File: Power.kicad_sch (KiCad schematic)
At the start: 26 parts, among them SW1 SHPHLD, U1 NPM1304-QEAA-R

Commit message: Changed a few preferences
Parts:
- C1, C10, C11, C2, C5, C6, C7, C8, C9: footprint Capacitor_SMD:C_1206_3216Metric_Pad1.33x1.80mm_HandSolder -> Capacitor_SMD:C_0603_1608Metric
- D1, D2, D3: footprint LED_SMD:LED_1206_3216Metric_Pad1.42x1.75mm_HandSolder -> LED_SMD:LED_0603_1608Metric
- R1, R10, R2, R3, R7, R8, R9: footprint Resistor_SMD:R_1206_3216Metric_Pad1.30x1.75mm_HandSolder -> Resistor_SMD:R_0603_1608Metric
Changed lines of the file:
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@@
 			)
 		)
-		(property "Footprint" "Capacitor_SMD:C_1206_3216Metric_Pad1.33x1.80mm_HandSolder"
+		(property "Footprint" "Capacitor_SMD:C_0603_1608Metric"
 			(at 214.3252 100.33 0)
 			(hide yes)
@@
 			)
 		)
-		(property "Footprint" "Resistor_SMD:R_1206_3216Metric_Pad1.30x1.75mm_HandSolder"
+		(property "Footprint" "Resistor_SMD:R_0603_1608Metric"
 			(at 203.2 81.28 0)
 			(hide yes)
@@
 			)
 		)
-		(property "Footprint" "Capacitor_SMD:C_1206_3216Metric_Pad1.33x1.80mm_HandSolder"
+		(property "Footprint" "Capacitor_SMD:C_0603_1608Metric"
 			(at 195.2752 58.42 0)
 			(hide yes)
@@
 			)
 		)
-		(property "Footprint" "Capacitor_SMD:C_1206_3216Metric_Pad1.33x1.80mm_HandSolder"
+		(property "Footprint" "Capacitor_SMD:C_0603_1608Metric"
 			(at 223.52 143.2052 0)
 			(hide yes)
@@
 			)
 		)
-		(property "Footprint" "LED_SMD:LED_1206_3216Metric_Pad1.42x1.75mm_HandSolder"
+		(property "Footprint" "LED_SMD:LED_0603_1608Metric"
 			(at 193.04 73.66 90)
 			(hide yes)
@@
 			)
 		)
-		(property "Footprint" "Resistor_SMD:R_1206_3216Metric_Pad1.30x1.75mm_HandSolder"
+		(property "Footprint" "Resistor_SMD:R_0603_1608Metric"
 			(at 106.172 107.95 90)
 			(hide yes)
@@
 			)
 		)
-		(property "Footprint" "Capacitor_SMD:C_1206_3216Metric_Pad1.33x1.80mm_HandSolder"
+		(property "Footprint" "Capacitor_SMD:C_0603_1608Metric"
 			(at 98.7552 81.28 0)
 			(hide yes)
@@
 			)
 		)
-		(property "Footprint" "Capacitor_SMD:C_1206_3216Metric_Pad1.33x1.80mm_HandSolder"
+		(property "Footprint" "Capacitor_SMD:C_0603_1608Metric"
 			(at 223.52 132.3848 0)
 			(hide yes)
@@
 			)
 		)
-		(property "Footprint" "Capacitor_SMD:C_1206_3216Metric_Pad1.33x1.80mm_HandSolder"
+		(property "Footprint" "Capacitor_SMD:C_0603_1608Metric"
 			(at 237.1852 100.33 0)
 			(hide yes)
@@
 			)
 		)
-		(property "Footprint" "Capacitor_SMD:C_1206_3216Metric_Pad1.33x1.80mm_HandSolder"
+		(property "Footprint" "Capacitor_SMD:C_0603_1608Metric"
 			(at 94.9452 63.5 0)
 			(hide yes)
@@
 			)
 		)
-		(property "Footprint" "Resistor_SMD:R_1206_3216Metric_Pad1.30x1.75mm_HandSolder"
+		(property "Footprint" "Resistor_SMD:R_0603_1608Metric"
 			(at 203.2 88.9 0)
 			(hide yes)
@@
 			)
 		)
-		(property "Footprint" "Resistor_SMD:R_1206_3216Metric_Pad1.30x1.75mm_HandSolder"
+		(property "Footprint" "Resistor_SMD:R_0603_1608Metric"
 			(at 177.292 110.49 90)
 			(hide yes)
@@
 			)
 		)
-		(property "Footprint" "LED_SMD:LED_1206_3216Metric_Pad1.42x1.75mm_HandSolder"
+		(property "Footprint" "LED_SMD:LED_0603_1608Metric"
 			(at 193.04 88.9 90)
 			(hide yes)
@@
 			)
 		)
-		(property "Footprint" "Capacitor_SMD:C_1206_3216Metric_Pad1.33x1.80mm_HandSolder"
+		(property "Footprint" "Capacitor_SMD:C_0603_1608Metric"
 			(at 225.7552 100.33 0)
 			(hide yes)
@@
 			)
 		)
-		(property "Footprint" "Resistor_SMD:R_1206_3216Metric_Pad1.30x1.75mm_HandSolder"
+		(property "Footprint" "Resistor_SMD:R_0603_1608Metric"
 			(at 83.312 102.87 90)
 			(hide yes)
@@
 			)
 		)
-		(property "Footprint" "LED_SMD:LED_1206_3216Metric_Pad1.42x1.75mm_HandSolder"
+		(property "Footprint" "LED_SMD:LED_0603_1608Metric"
 			(at 193.04 81.28 90)
 			(hide yes)
@@
 			)
 		)
-		(property "Footprint" "Resistor_SMD:R_1206_3216Metric_Pad1.30x1.75mm_HandSolder"
+		(property "Footprint" "Resistor_SMD:R_0603_1608Metric"
 			(at 75.692 102.87 90)
 			(hide yes)
@@
 			)
 		)
-		(property "Footprint" "Resistor_SMD:R_1206_3216Metric_Pad1.30x1.75mm_HandSolder"
+		(property "Footprint" "Resistor_SMD:R_0603_1608Metric"
 			(at 203.2 73.66 0)
 			(hide yes)
@@
 			)
 		)
-		(property "Footprint" "Capacitor_SMD:C_1206_3216Metric_Pad1.33x1.80mm_HandSolder"
+		(property "Footprint" "Capacitor_SMD:C_0603_1608Metric"
 			(at 162.56 133.0452 0)
 			(hide yes)

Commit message: Finished preliminary project schematics and architecture
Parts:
- NT1, NT2: footprint NetTie:NetTie-2_SMD_Pad0.5mm -> NetTie:NetTie-2_SMD_Pad2.0mm
- renumbered C1 to C3, C2 to C4, L1 to L2, L2 to L3, R7 to R4, R8 to R5, R9 to R6, R10 to R7, U1 to U3
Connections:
- net NTC is gone; now on net GND: U3.18 (NTC)

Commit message: Edited ci.yaml
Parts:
- removed BT1: 1S Lipo, Connector_JST:JST_XH_B2B-XH-A_1x02_P2.50mm_Vertical, symbol Device:Battery_Cell
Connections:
- net CC1: now also U3.23 (CC1); no longer U3.24 (CC2)
- net CC2: now also U3.24 (CC2); no longer U3.23 (CC1)

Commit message: Cleaned up
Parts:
- renumbered C11 to C10, C5 to C11, C8 to C12, C9 to C13, C6 to C5, C3 to C6, C4 to C7, C7 to C8, C10 to C9, L3 to L2, L2 to L3, R4 to R10, R5 to R4, R6 to R5, R7 to R6, R1 to R7, R2 to R8, R3 to R9, SW1 to SW3, U3 to U2

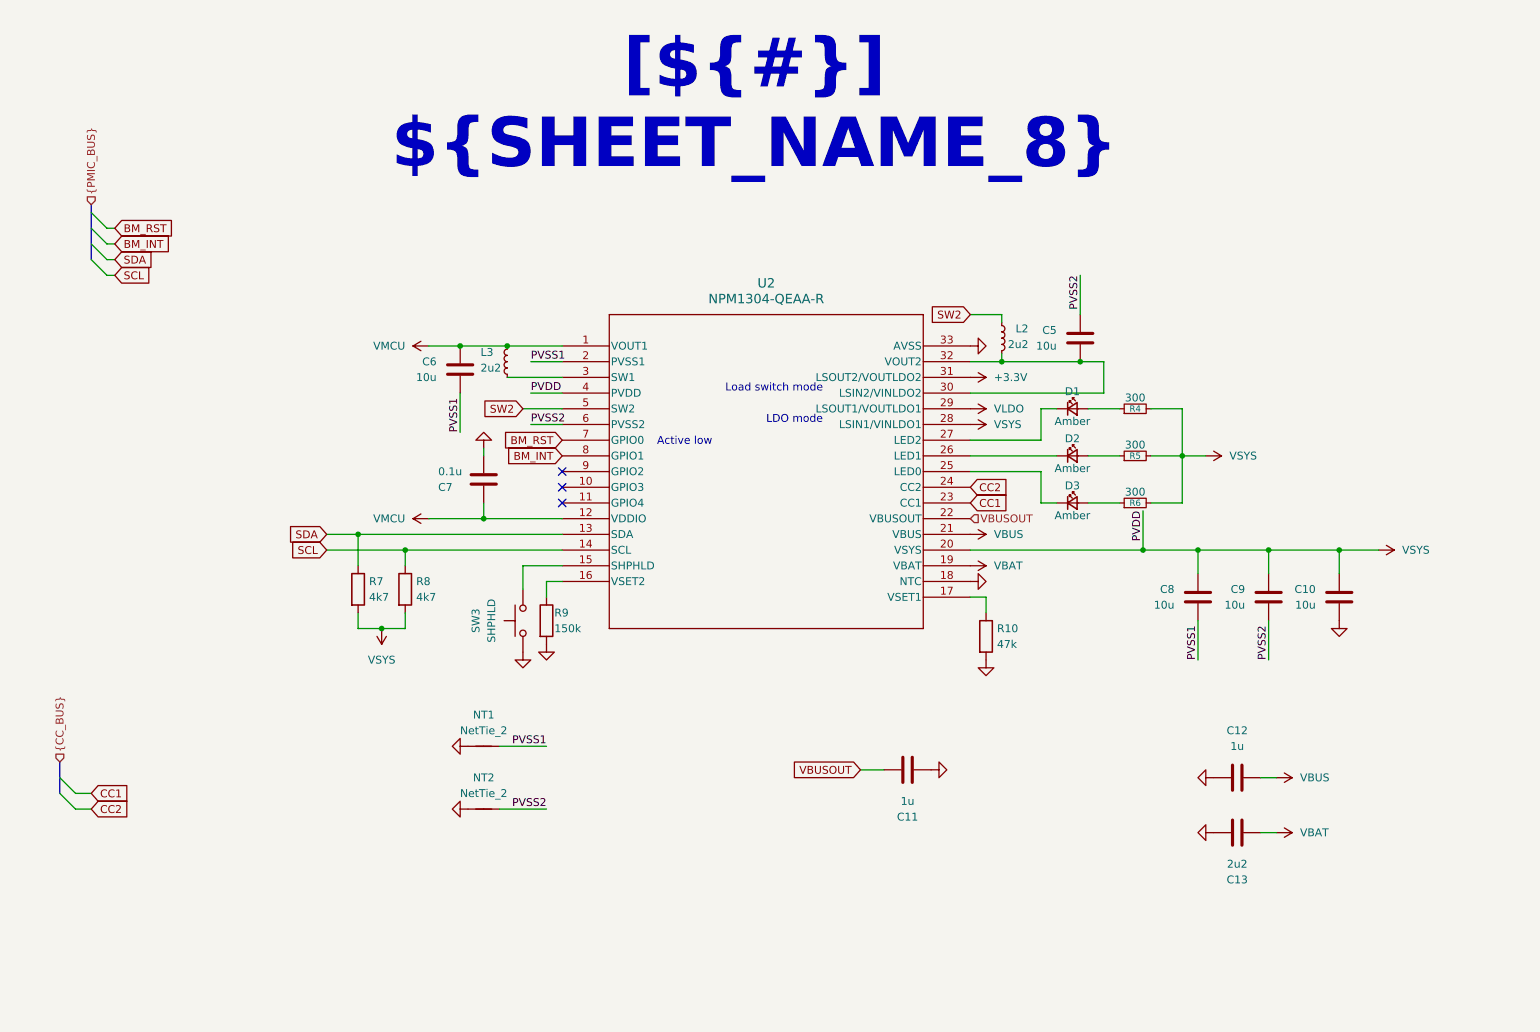
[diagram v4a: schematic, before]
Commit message: Minor schematic adjustments
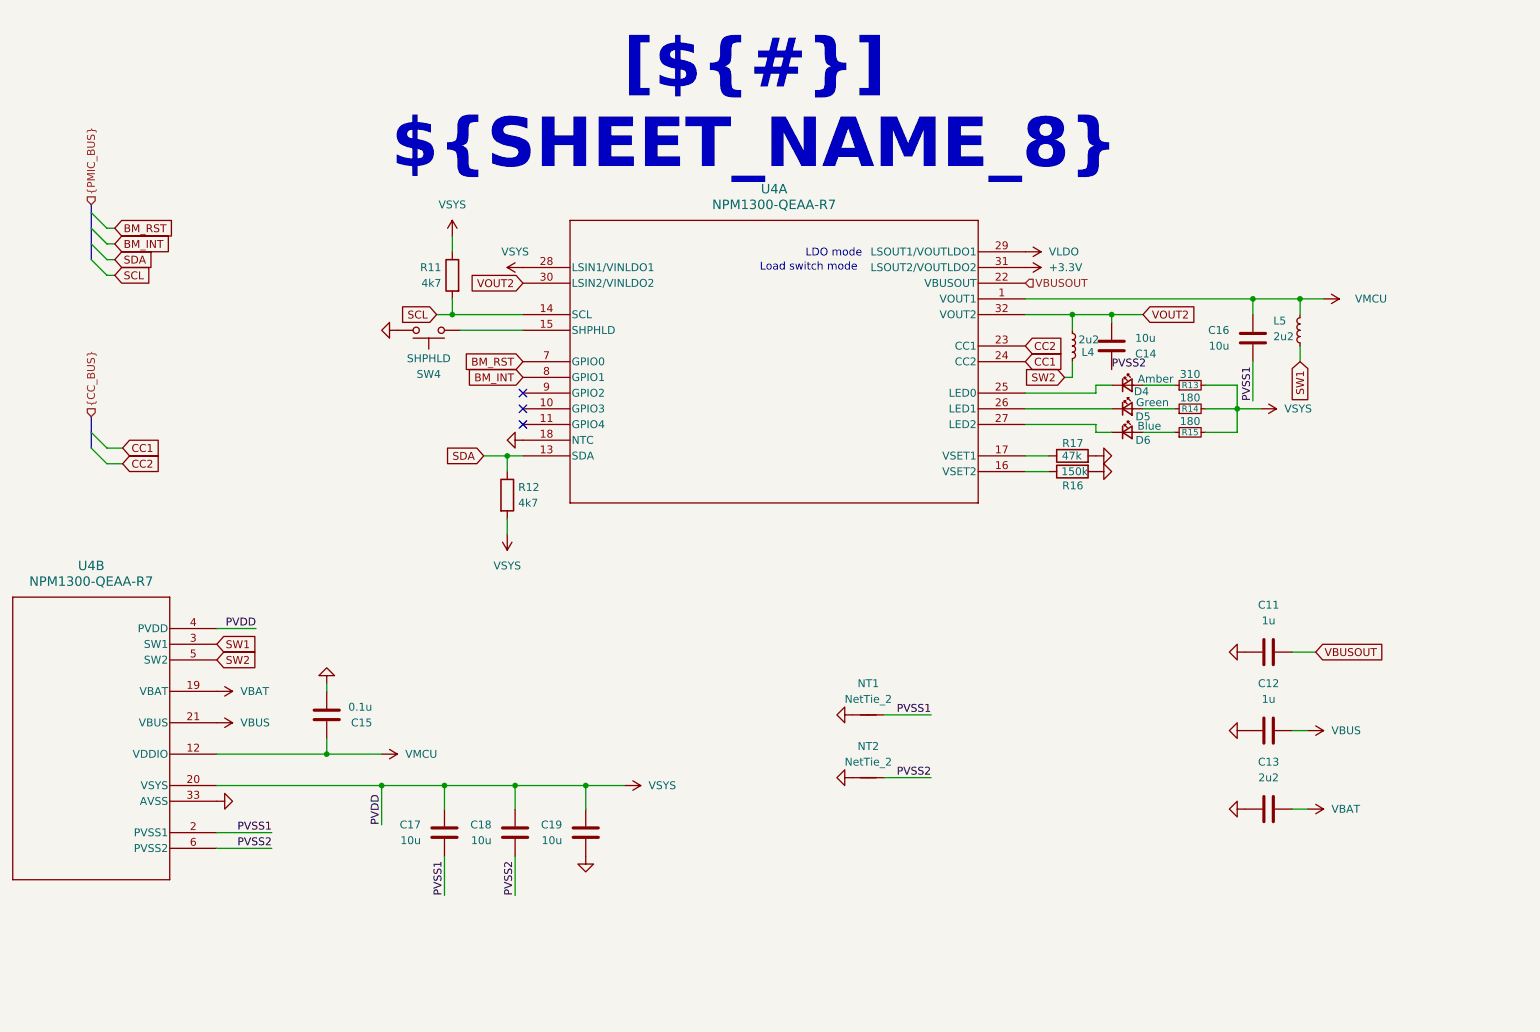
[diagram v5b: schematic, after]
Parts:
- removed C10, C5, C6, C8, C9: 10u, Capacitor_SMD:C_0603_1608Metric, symbol Device:C
- removed C7: 0.1u, Capacitor_SMD:C_0603_1608Metric, symbol Device:C
- removed D1, D2, D3: Amber, LED_SMD:LED_0603_1608Metric, symbol Device:LED_Small
- removed L2, L3: 2u2, Inductor_SMD:L_0805_2012Metric_Pad1.05x1.20mm_HandSolder, symbol Device:L_Small
- removed R10: 47k, Resistor_SMD:R_0603_1608Metric, symbol Device:R
- removed R4, R5, R6: 300, Resistor_SMD:R_0603_1608Metric, symbol Device:R_Small
- removed R7, R8: 4k7, Resistor_SMD:R_0603_1608Metric, symbol Device:R
- removed R9: 150k, Resistor_SMD:R_0603_1608Metric, symbol Device:R
- removed SW3: SHPHLD, Button_Switch_SMD:SW_Push_1P1T_NO_CK_KMR2, symbol Switch:SW_Push
- removed U2: NPM1304-QEAA-R, Project_Components:QFN32_5X5_NOR, symbol 2026-05-19_19-41-51:NPM1300-QEAA-R7
- added C14, C16, C17, C18, C19: 10u, Capacitor_SMD:C_0603_1608Metric, symbol Device:C
- added C15: 0.1u, Capacitor_SMD:C_0603_1608Metric, symbol Device:C
- added D4: Amber, LED_SMD:LED_0603_1608Metric, symbol Device:LED_Small
- added D5: Green, LED_SMD:LED_0603_1608Metric, symbol Device:LED_Small
- added D6: Blue, LED_SMD:LED_0603_1608Metric, symbol Device:LED_Small
- added L4, L5: 2u2, Inductor_SMD:L_0805_2012Metric_Pad1.05x1.20mm_HandSolder, symbol Device:L_Small
- added R11, R12: 4k7, Resistor_SMD:R_0603_1608Metric, symbol Device:R
- added R13: 310, Resistor_SMD:R_0603_1608Metric, symbol Device:R_Small
- added R14, R15: 180, Resistor_SMD:R_0603_1608Metric, symbol Device:R_Small
- added R16: 150k, Resistor_SMD:R_0603_1608Metric, symbol Device:R
- added R17: 47k, Resistor_SMD:R_0603_1608Metric, symbol Device:R
- added SW4: SHPHLD, Button_Switch_SMD:SW_Push_1P1T_NO_CK_KMR2, symbol Switch:SW_Push
- added U4: NPM1300-QEAA-R7, Project_Components:QFN32_5X5_NOR, symbol Project_Components:NPM1300-QEAA-R7
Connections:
- net +3.3V: now also U4.31 (LSOUT2/VOUTLDO2)
- net BM_INT: now also U4.8 (GPIO1)
- net BM_RST: now also U4.7 (GPIO0)
- net CC1: now also U4.24 (CC2)
- net CC2: now also U4.23 (CC1)
- net GND: now also C15.2, C19.1, R16.2, R17.2, SW4.2, U4.18 (NTC), U4.33 (AVSS)
- net PVSS1: now also C16.1, C17.1, U4.2 (PVSS1)
- net PVSS2: now also C14.2, C18.1, U4.6 (PVSS2)
- net SCL: now also R11.2, U4.14 (SCL)
- net SDA: now also R12.1, U4.13 (SDA)
- net SW2: now also L4.2, U4.5 (SW2)
- net VBAT: now also U4.19 (VBAT)
- net VBUS: now also U4.21 (VBUS)
- net VBUSOUT: now also U4.22 (VBUSOUT)
- net VLDO: now also U4.29 (LSOUT1/VOUTLDO1)
- net VMCU: now also C15.1, C16.2, L5.2, U4.1 (VOUT1), U4.12 (VDDIO)
- net VSYS: now also C17.2, C18.2, C19.2, R11.1, R12.2, R13.2, R14.2, R15.2, U4.20 (VSYS), U4.28 (LSIN1/VINLDO1), U4.4 (PVDD)
- new net: D4.2 (A), R13.1
- new net: SW4.1, U4.15 (SHPHLD)
- new net: D4.1 (K), U4.25 (LED0)
- new net: R17.1, U4.17 (VSET1)
- new net: R16.1, U4.16 (VSET2)
- new net: D5.1 (K), U4.26 (LED1)
- new net: D5.2 (A), R14.1
- new net: D6.2 (A), R15.1
- new net: D6.1 (K), U4.27 (LED2)
- new net SW1: L5.1, U4.3 (SW1)
- new net VOUT2: C14.1, L4.1, U4.30 (LSIN2/VINLDO2), U4.32 (VOUT2)
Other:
- note removed: "Active low"
- moved on the sheet: C11, C12, C13, NT1, NT2
